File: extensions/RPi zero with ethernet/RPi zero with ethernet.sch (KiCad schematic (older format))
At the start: 36 parts, among them CON1 HR911105A, M1 MH_M3, M2 MH_M3, M3 MH_M3, M4 MH_M3, P1 CONN_01X02, P2 CONN_01X20, P3 CONN_02X20, P4 CONN_02X05, P5 CONN_01X20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

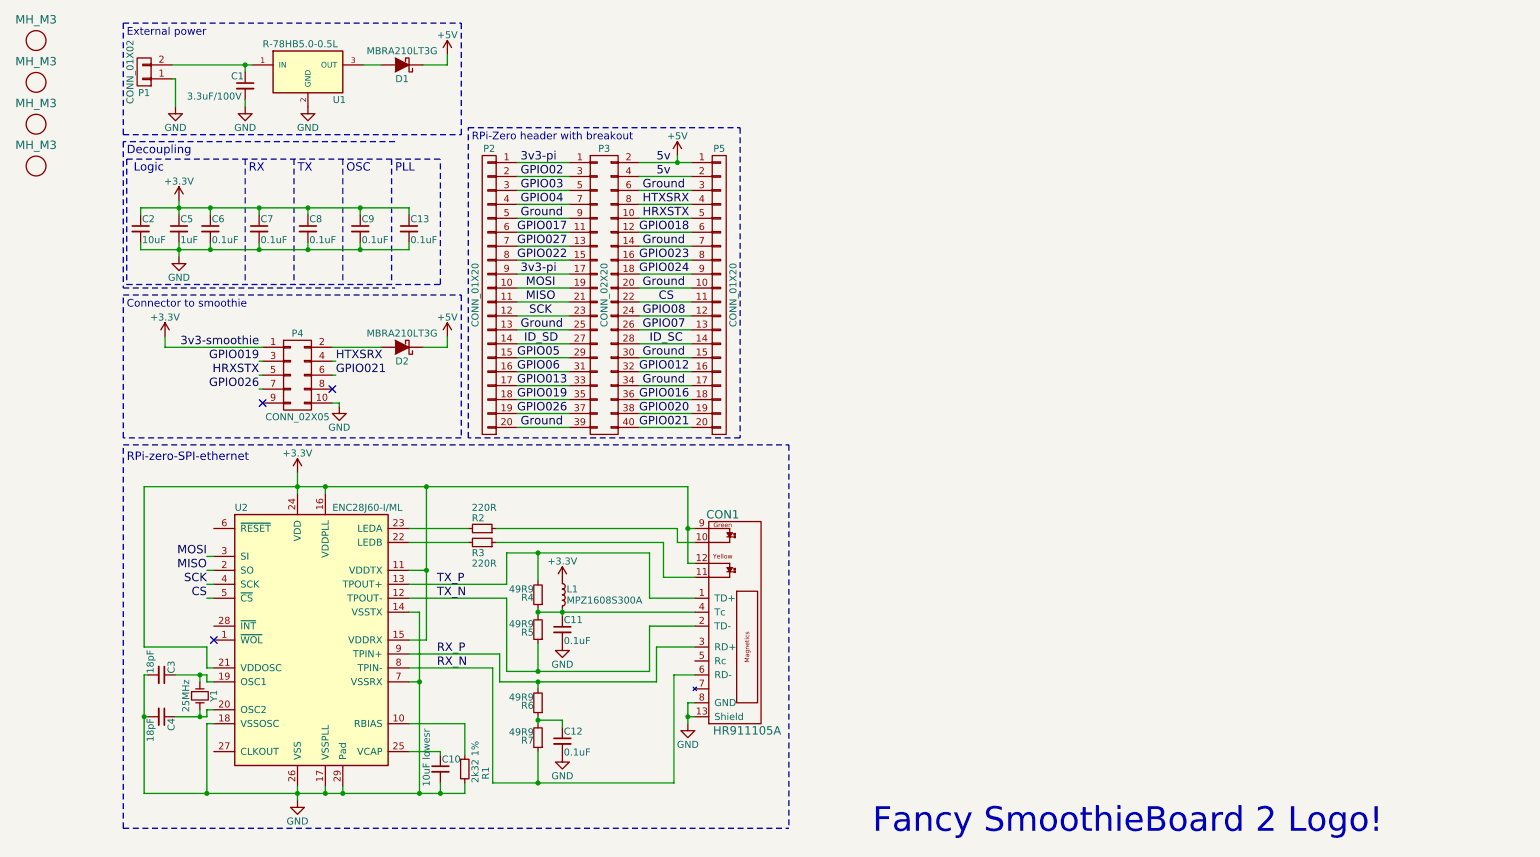
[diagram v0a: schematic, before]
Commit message: Fit both Pi adapters to one pcb
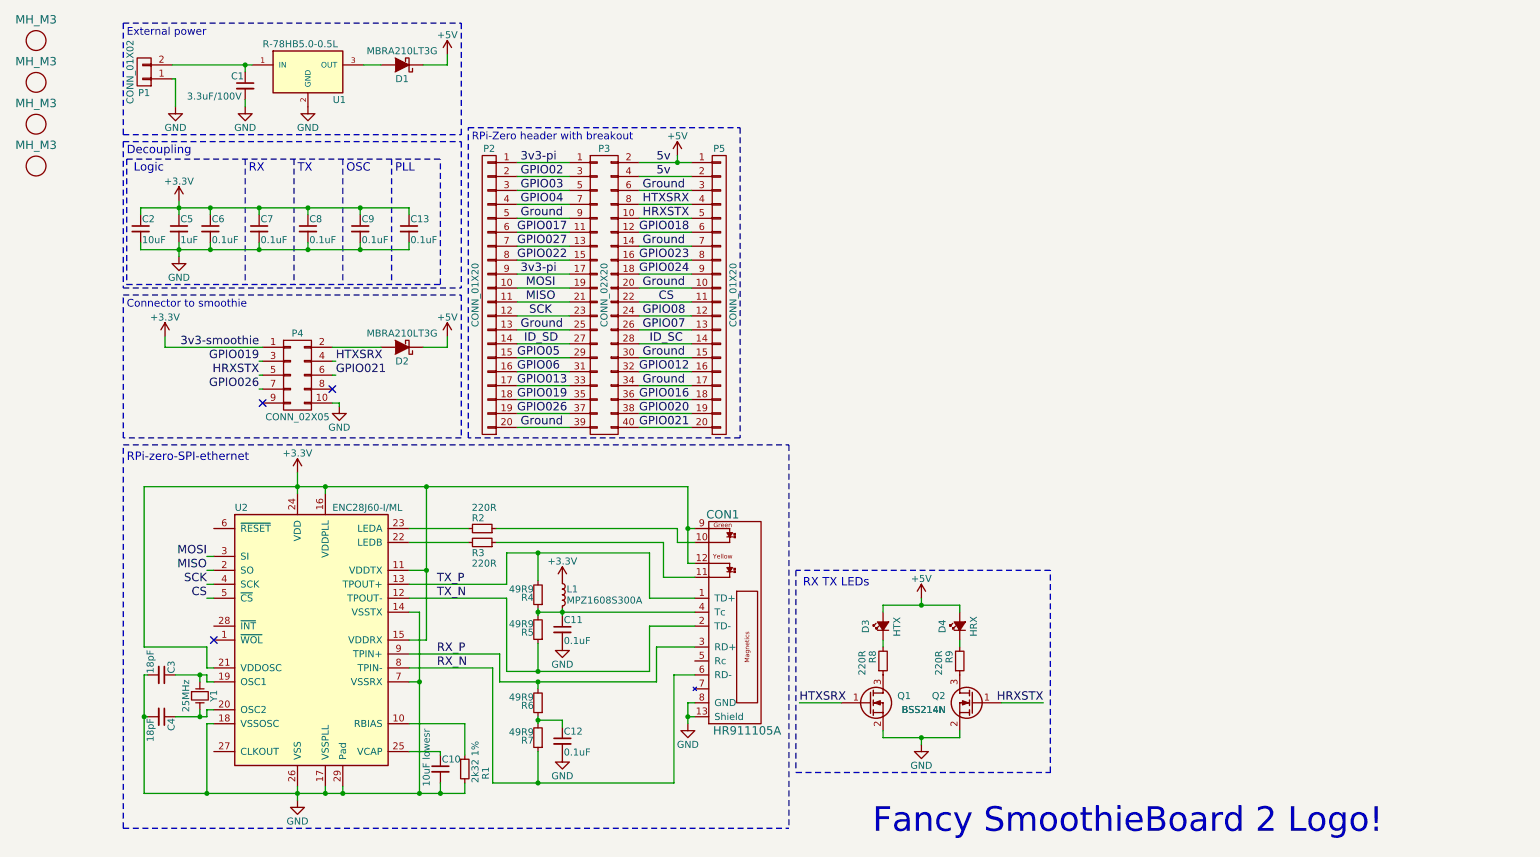
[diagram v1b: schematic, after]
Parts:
- added D3: HTX, Diodes_SMD:D_0805, symbol Led_Small
- added D4: HRX, Diodes_SMD:D_0805, symbol Led_Small
- added Q1, Q2: BSS214N, TO_SOT_Packages_SMD:SOT-23, symbol Q_NMOS_GSD
- added R8, R9: 220R, Resistors_SMD:R_0603, symbol R_Small
- C1: footprint Resistors_SMD:R_1210 -> Capacitors_SMD:C_1206
- C10: footprint Capacitors_SMD:C_0805 -> Capacitors_SMD:C_0603
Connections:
- net +5V: now also D3.2 (A), D4.2 (A)
- net GND: now also Q1.2 (S), Q2.2 (S)
- net HRXSTX: now also Q2.1 (G)
- net HTXSRX: now also Q1.1 (G)
- new net: D3.1 (K), R8.2
- new net: D4.1 (K), R9.2
- new net: Q1.3 (D), R8.1
- new net: Q2.3 (D), R9.1
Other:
- note added: "RX TX LEDs"
